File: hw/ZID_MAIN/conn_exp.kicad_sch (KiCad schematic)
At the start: 64 parts, among them J10 USB-C PWR ONLY, J8 BRK-EXP-UNIT, J9 Z80-TARGET, U24 74AHCT125

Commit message: PCB layout 2
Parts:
- added LED10: LED ORANGE, LED_THT:LED_D3.0mm, symbol Device:LED
- added R37: 1.2k, Resistor_SMD:R_0805_2012Metric, symbol Device:R_Small_US
- renumbered D1 to LED1, D2 to LED2, D3 to LED3, D4 to LED4
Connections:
- net +5V: now also R37.2
- net GND: now also LED10.1 (K)
- new net: LED10.2 (A), R37.1
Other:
- moved on the sheet: SPARE1

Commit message: POD start PCB
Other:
- moved on the sheet: SPARE1
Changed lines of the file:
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@@
 	(symbol
 		(lib_id "AES_Library:SPARE-16-AES")
-		(at 62.23 292.1 0)
+		(at 81.28 290.83 0)
 		(unit 1)
 		(exclude_from_sim no)
@@
 		(dnp no)
 		(property "Reference" "SPARE1"
-			(at 62.484 303.276 0)
+			(at 81.534 302.006 0)
 			(effects
 				(font
@@
 		)
 		(property "Value" "~"
-			(at 62.484 292.1 0)
+			(at 81.534 290.83 0)
 			(effects
 				(font
@@
 		)
 		(property "Footprint" "AES_Library:SPARE-and-SOIC-16-AES"
-			(at 62.23 292.1 0)
+			(at 81.28 290.83 0)
 			(effects
 				(font
@@
 		)
 		(property "Datasheet" ""
-			(at 62.23 292.1 0)
+			(at 81.28 290.83 0)
 			(effects
 				(font
@@
 		)
 		(property "Description" "Symbol to use when placing spares on a PCB. Match with one of the 16 pin footprints."
-			(at 62.23 292.1 0)
+			(at 81.28 290.83 0)
 			(effects
 				(font
@@
 		)
 		(property "Function" ""
-			(at 62.23 292.1 0)
+			(at 81.28 290.83 0)
 			(effects
 				(font

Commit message: PCB Main: layout 20250411a
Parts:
- added J11: Conn_01x08, Connector_PinHeader_2.54mm:PinHeader_1x08_P2.54mm_Vertical, symbol Connector_Generic:Conn_01x08
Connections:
- net +5V: now also J8.40 (PWR); no longer J8.29 (PWR), J8.31 (PWR), J8.33 (PWR)
- net D7_B: now also J8.28 (AEDI1); no longer J8.30 (AEDI1)
- net GND: now also J8.38 (GND); no longer J8.35 (GND), J8.37 (GND)
- net TD0: now also J11.1 (Pin_1)
- net TD1: now also J11.2 (Pin_2)
- net TD2: now also J11.3 (Pin_3)
- net TD3: now also J11.4 (Pin_4)
- net TD4: now also J11.5 (Pin_5)
- net TD5: now also J11.6 (Pin_6)
- net TD6: now also J11.7 (Pin_7)
- net TD7: now also J11.8 (Pin_8)
- net TIORQ-: now also J8.33 (~{IORQ})
- net TM1-: now also J8.29 (~{M1})
- net TMREQ-: now also J8.31 (~{MREQ})
- net TRD-: now also J8.37 (~{RD})
- net TWR-: now also J8.35 (~{WR})
- no-connect marks 18 -> 16
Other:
- moved on the sheet: JP5, R21, R22

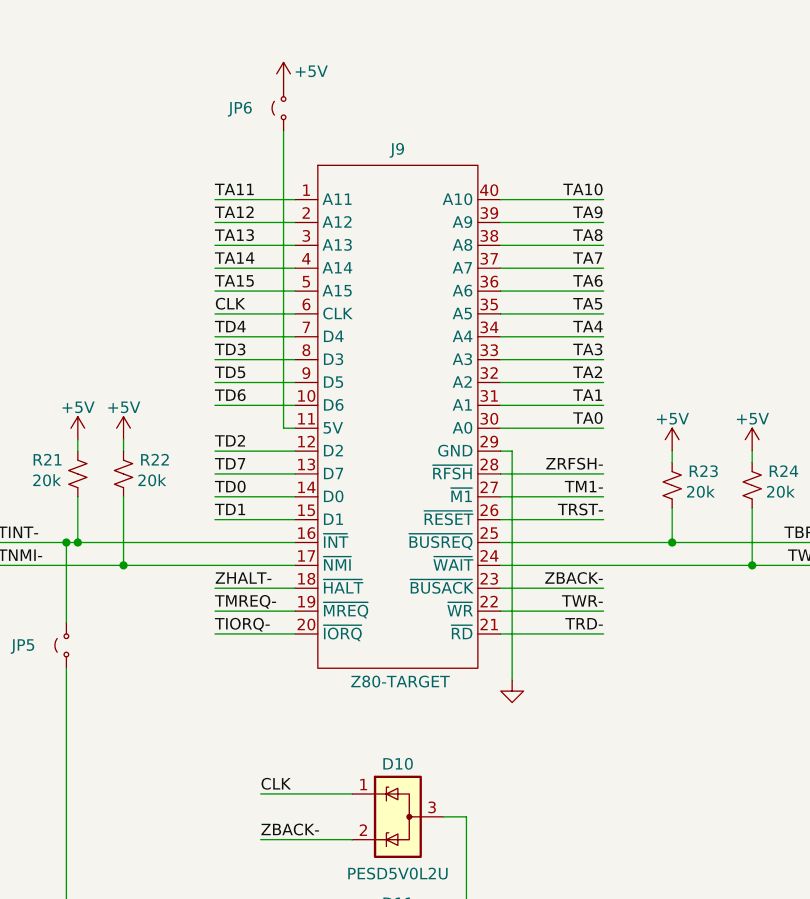
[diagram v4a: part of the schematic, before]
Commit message: POD PCB increase GND trace width
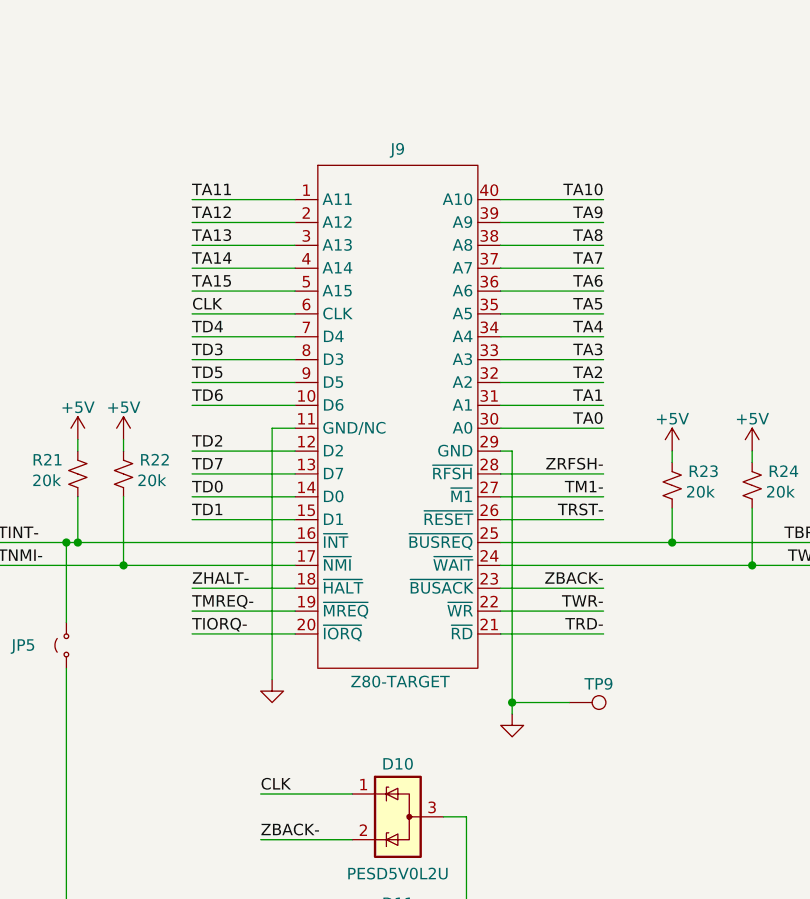
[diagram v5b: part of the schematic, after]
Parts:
- removed JP6: Jumper_2_Small_Open, Connector_PinHeader_2.00mm:PinHeader_1x02_P2.00mm_Vertical, symbol Jumper:Jumper_2_Small_Open
- added TP9: TestPoint, Connector_PinHeader_2.54mm:PinHeader_1x01_P2.54mm_Vertical, symbol Connector:TestPoint
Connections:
- net GND: now also J9.11 (GND/NC), TP9.1

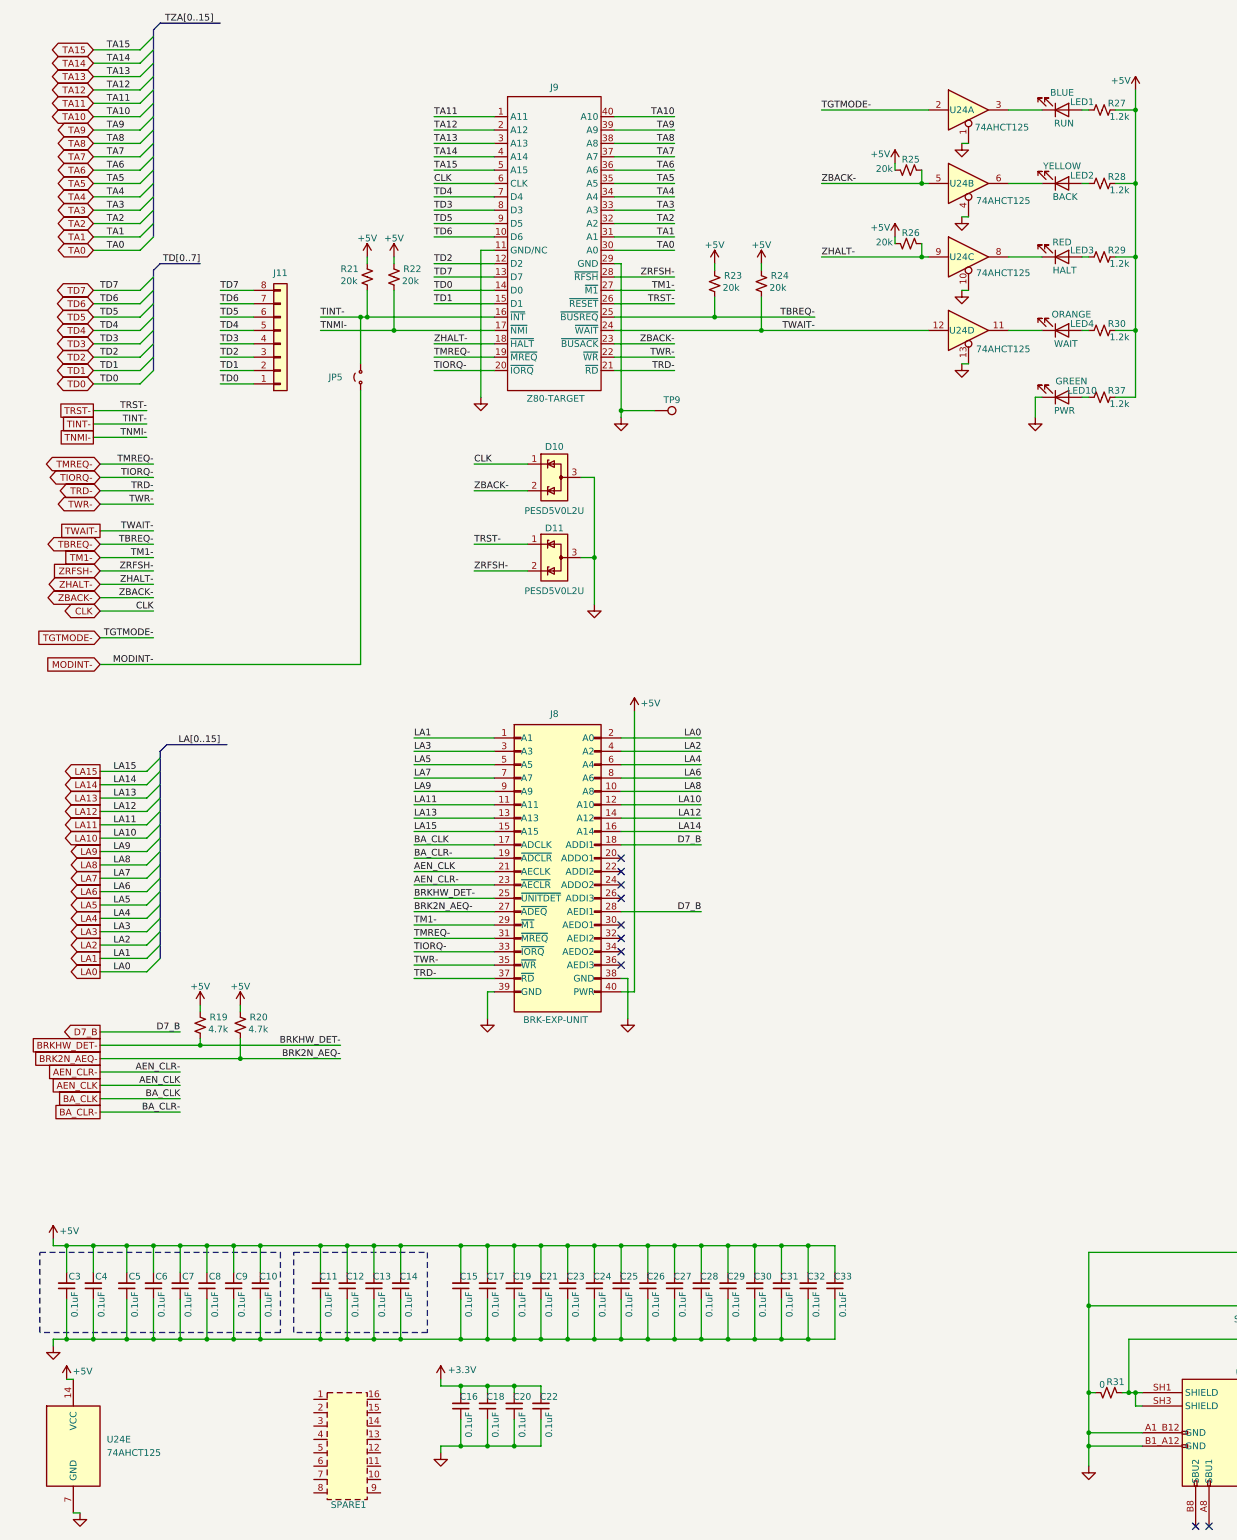
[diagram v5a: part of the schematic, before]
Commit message: Exp-BP: Add display
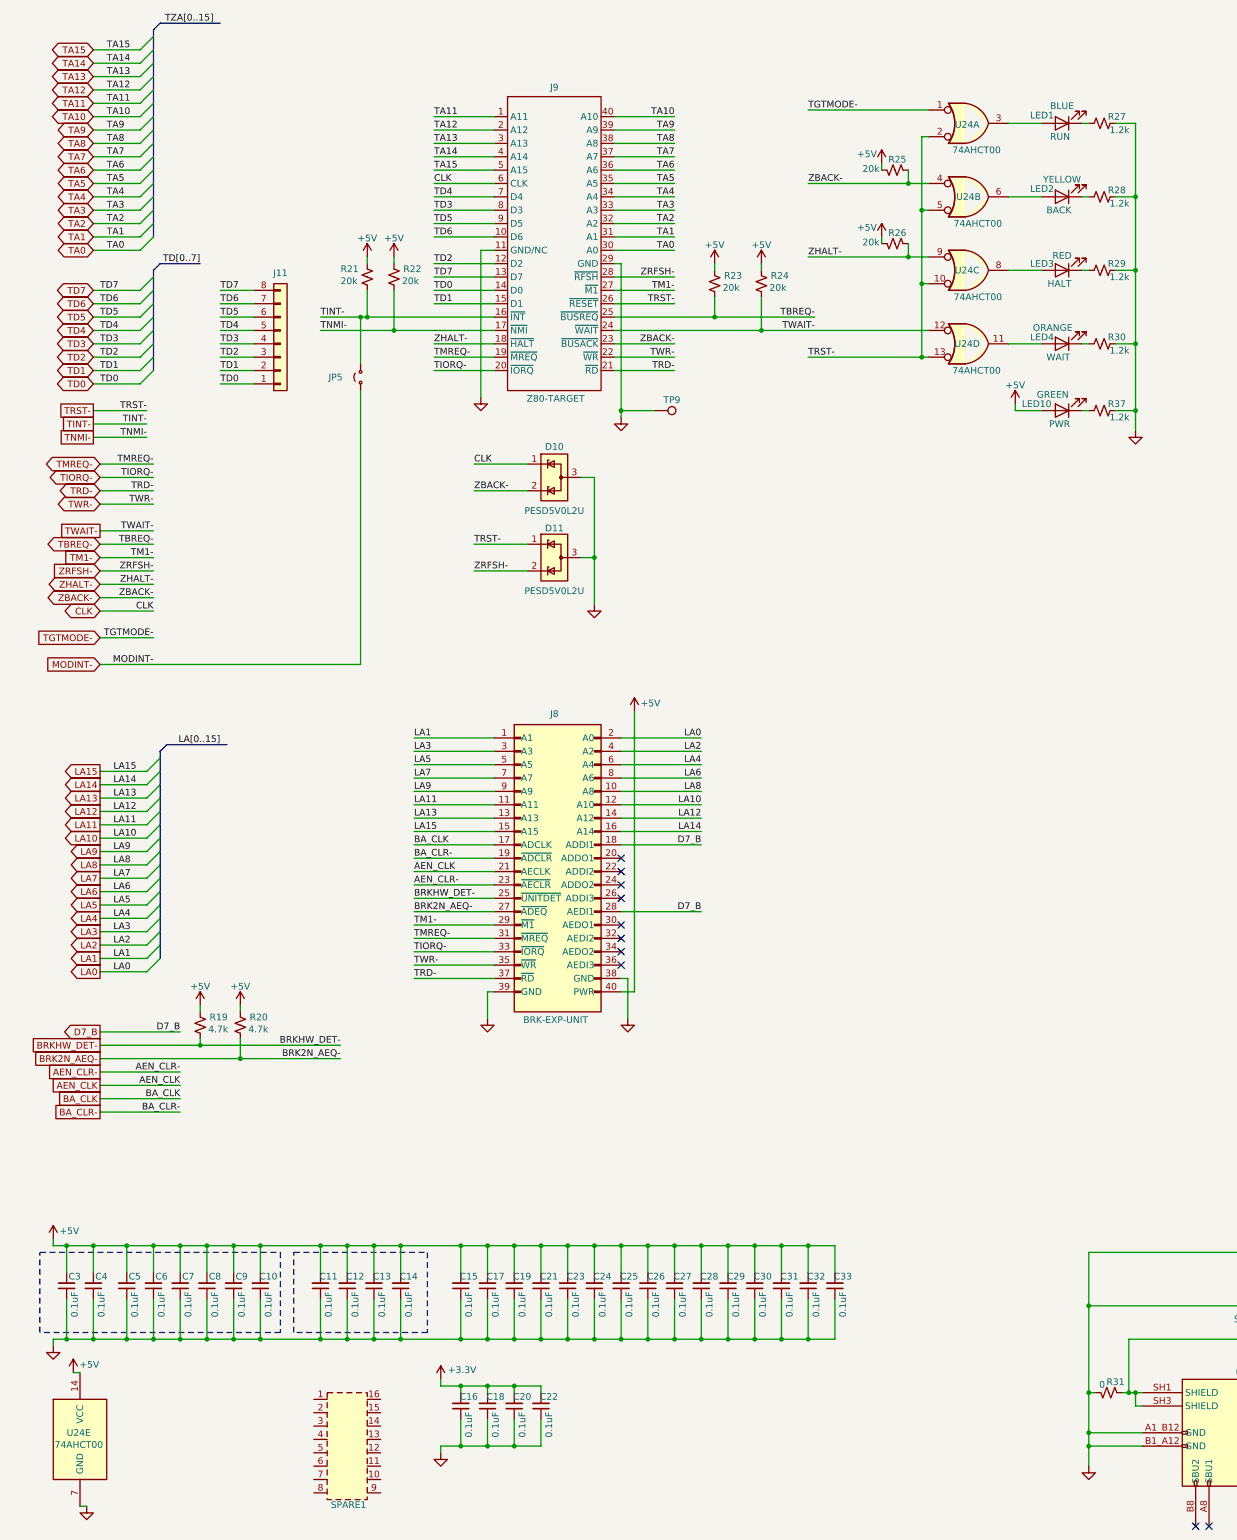
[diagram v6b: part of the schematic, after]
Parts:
- removed U24: 74AHCT125, Package_SO:SOIC-14_3.9x8.7mm_P1.27mm, symbol 74xx:74LVC125
- added U24: 74AHCT00, Package_SO:SOIC-14_3.9x8.7mm_P1.27mm, symbol 74xx:74HCT00
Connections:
- net +5V: now also LED10.2 (A), U24.14 (VCC); no longer R27.2, R28.2, R29.2, R30.2, R37.2
- net GND: now also R27.2, R28.2, R29.2, R30.2, R37.2, U24.7 (GND); no longer LED10.1 (K)
- net TGTMODE-: now also U24.1
- net TRST-: now also U24.10, U24.13, U24.2, U24.5
- net TWAIT-: now also U24.12
- net ZBACK-: now also U24.4
- net ZHALT-: now also U24.9
- net at R37.1: now also LED10.1 (K); no longer LED10.2 (A)
- net at LED4.1 (K): now also R30.1
- net at LED4.2 (A): now also U24.11; no longer R30.1
- net at LED3.1 (K): now also R29.1
- net at LED1.1 (K): now also R27.1
- net at LED1.2 (A): now also U24.3; no longer R27.1
- net at LED3.2 (A): now also U24.8; no longer R29.1
- net at LED2.1 (K): now also R28.1
- net at LED2.2 (A): now also U24.6; no longer R28.1
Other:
- moved on the sheet: LED1, LED10, LED2, LED3, LED4, R25, R26, R27, R28, R29, R30, R37
